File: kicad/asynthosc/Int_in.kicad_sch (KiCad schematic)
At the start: 7 parts, among them J8 AudioJack3, Q1 Q_NPN_BEC, SW10 SW_MEC_5G_LED

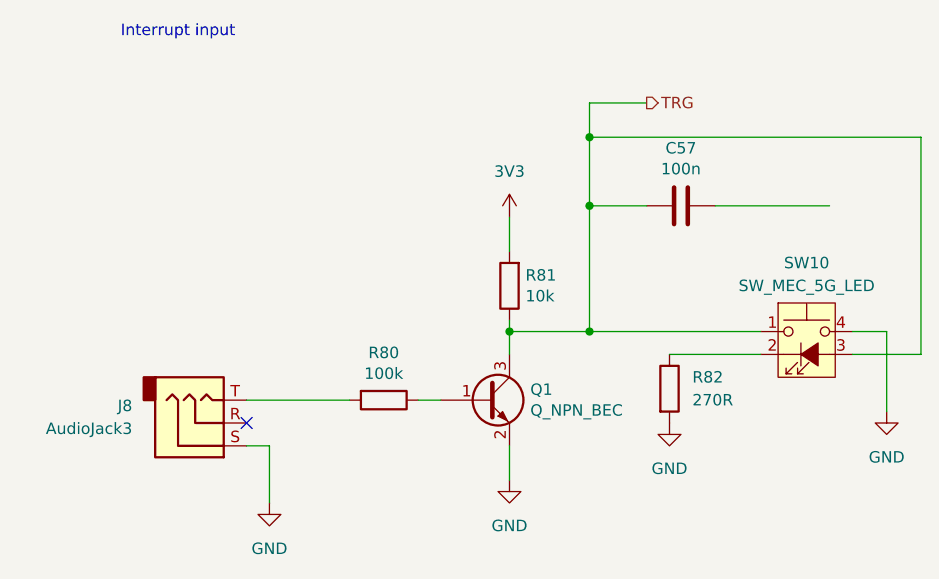
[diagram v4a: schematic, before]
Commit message: bom: update bom for lcsc
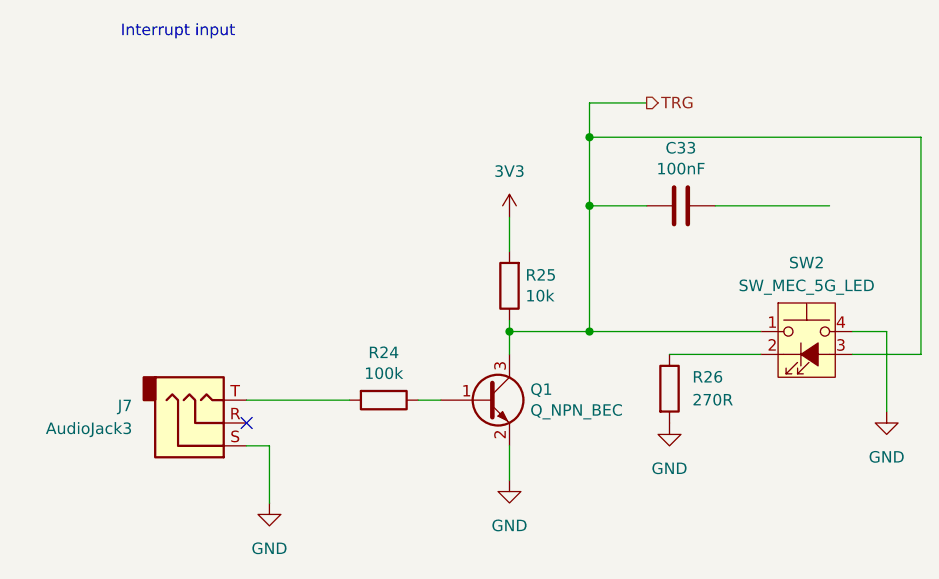
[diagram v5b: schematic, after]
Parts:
- C33: renamed from C57; value 100n -> 100nF
- R24: renamed from R80; RefNum (none) -> _generic_
- R25: renamed from R81; RefNum (none) -> _generic_
- R26: renamed from R82; RefNum (none) -> _generic_
- renumbered J8 to J7, SW10 to SW2
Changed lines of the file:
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@@
 		(dnp no)
 		(fields_autoplaced yes)
-		(property "Reference" "#PWR0137"
+		(property "Reference" "#PWR063"
 			(at 58.42 83.82 0)
 			(effects
@@
 			(project "asynthosc"
 				(path "/d73e377a-a016-415f-8824-91cc6e4907b9/5f8430bb-1923-4d76-b418-f207310879ec/00719137-6b38-42a6-b28f-e4711c0869df"
-					(reference "#PWR0137")
-					(unit 1)
-				)
-				(path "/d73e377a-a016-415f-8824-91cc6e4907b9/5f8430bb-1923-4d76-b418-f207310879ec/1b493739-e50b-4e48-bad0-48b50a96f04e"
-					(reference "#PWR092")
+					(reference "#PWR063")
+					(unit 1)
+				)
+				(path "/d73e377a-a016-415f-8824-91cc6e4907b9/5f8430bb-1923-4d76-b418-f207310879ec/1b493739-e50b-4e48-bad0-48b50a96f04e"
+					(reference "#PWR086")
 					(unit 1)
 				)
@@
 		(dnp no)
 		(fields_autoplaced yes)
-		(property "Reference" "#PWR0140"
+		(property "Reference" "#PWR066"
 			(at 102.87 74.93 0)
 			(effects
@@
 			(project "asynthosc"
 				(path "/d73e377a-a016-415f-8824-91cc6e4907b9/5f8430bb-1923-4d76-b418-f207310879ec/00719137-6b38-42a6-b28f-e4711c0869df"
-					(reference "#PWR0140")
-					(unit 1)
-				)
-				(path "/d73e377a-a016-415f-8824-91cc6e4907b9/5f8430bb-1923-4d76-b418-f207310879ec/1b493739-e50b-4e48-bad0-48b50a96f04e"
-					(reference "#PWR0132")
+					(reference "#PWR066")
+					(unit 1)
+				)
+				(path "/d73e377a-a016-415f-8824-91cc6e4907b9/5f8430bb-1923-4d76-b418-f207310879ec/1b493739-e50b-4e48-bad0-48b50a96f04e"
+					(reference "#PWR089")
 					(unit 1)
 				)
@@
 		(dnp no)
 		(fields_autoplaced yes)
-		(property "Reference" "SW10"
+		(property "Reference" "SW2"
 			(at 118.11 50.8 0)
 			(effects
@@
 			(project "asynthosc"
 				(path "/d73e377a-a016-415f-8824-91cc6e4907b9/5f8430bb-1923-4d76-b418-f207310879ec/00719137-6b38-42a6-b28f-e4711c0869df"
-					(reference "SW10")
-					(unit 1)
-				)
-				(path "/d73e377a-a016-415f-8824-91cc6e4907b9/5f8430bb-1923-4d76-b418-f207310879ec/1b493739-e50b-4e48-bad0-48b50a96f04e"
-					(reference "SW7")
+					(reference "SW2")
+					(unit 1)
+				)
+				(path "/d73e377a-a016-415f-8824-91cc6e4907b9/5f8430bb-1923-4d76-b418-f207310879ec/1b493739-e50b-4e48-bad0-48b50a96f04e"
+					(reference "SW6")
 					(unit 1)
 				)
@@
 		(on_board yes)
 		(dnp no)
-		(property "Reference" "J8"
+		(property "Reference" "J7"
 			(at 43.18 66.6749 0)
 			(effects
@@
 			(project "asynthosc"
 				(path "/d73e377a-a016-415f-8824-91cc6e4907b9/5f8430bb-1923-4d76-b418-f207310879ec/00719137-6b38-42a6-b28f-e4711c0869df"
-					(reference "J8")
-					(unit 1)
-				)
-				(path "/d73e377a-a016-415f-8824-91cc6e4907b9/5f8430bb-1923-4d76-b418-f207310879ec/1b493739-e50b-4e48-bad0-48b50a96f04e"
-					(reference "J5")
+					(reference "J7")
+					(unit 1)
+				)
+				(path "/d73e377a-a016-415f-8824-91cc6e4907b9/5f8430bb-1923-4d76-b418-f207310879ec/1b493739-e50b-4e48-bad0-48b50a96f04e"
+					(reference "J11")
 					(unit 1)
 				)
@@
 		(on_board yes)
 		(dnp no)
-		(property "Reference" "R80"
+		(property "Reference" "R24"
 			(at 71.12 60.7822 90)
 			(effects
@@
 			)
 		)
+		(property "RefNum" "_generic_"
+			(at 71.12 66.04 0)
+			(effects
+				(font
+					(size 1.27 1.27)
+				)
+				(hide yes)
+			)
+		)
 		(pin "2"
 		)
@@
 			(project "asynthosc"
 				(path "/d73e377a-a016-415f-8824-91cc6e4907b9/5f8430bb-1923-4d76-b418-f207310879ec/00719137-6b38-42a6-b28f-e4711c0869df"
-					(reference "R80")
-					(unit 1)
-				)
-				(path "/d73e377a-a016-415f-8824-91cc6e4907b9/5f8430bb-1923-4d76-b418-f207310879ec/1b493739-e50b-4e48-bad0-48b50a96f04e"
-					(reference "R13")
+					(reference "R24")
+					(unit 1)
+				)
+				(path "/d73e377a-a016-415f-8824-91cc6e4907b9/5f8430bb-1923-4d76-b418-f207310879ec/1b493739-e50b-4e48-bad0-48b50a96f04e"
+					(reference "R45")
 					(unit 1)
 				)
@@
 		(dnp no)
 		(fields_autoplaced yes)
-		(property "Reference" "#PWR0139"
+		(property "Reference" "#PWR065"
 			(at 85.09 81.28 0)
 			(effects
@@
 			(project "asynthosc"
 				(path "/d73e377a-a016-415f-8824-91cc6e4907b9/5f8430bb-1923-4d76-b418-f207310879ec/00719137-6b38-42a6-b28f-e4711c0869df"
-					(reference "#PWR0139")
-					(unit 1)
-				)
-				(path "/d73e377a-a016-415f-8824-91cc6e4907b9/5f8430bb-1923-4d76-b418-f207310879ec/1b493739-e50b-4e48-bad0-48b50a96f04e"
-					(reference "#PWR031")
+					(reference "#PWR065")
+					(unit 1)
+				)
+				(path "/d73e377a-a016-415f-8824-91cc6e4907b9/5f8430bb-1923-4d76-b418-f207310879ec/1b493739-e50b-4e48-bad0-48b50a96f04e"
+					(reference "#PWR088")
 					(unit 1)
 				)
@@
 		(dnp no)
 		(fields_autoplaced yes)
-		(property "Reference" "#PWR0138"
+		(property "Reference" "#PWR064"
 			(at 85.09 49.53 0)
 			(effects
@@
 			(project "asynthosc"
 				(path "/d73e377a-a016-415f-8824-91cc6e4907b9/5f8430bb-1923-4d76-b418-f207310879ec/00719137-6b38-42a6-b28f-e4711c0869df"
-					(reference "#PWR0138")
-					(unit 1)
-				)
-				(path "/d73e377a-a016-415f-8824-91cc6e4907b9/5f8430bb-1923-4d76-b418-f207310879ec/1b493739-e50b-4e48-bad0-48b50a96f04e"
-					(reference "#PWR030")
+					(reference "#PWR064")
+					(unit 1)
+				)
+				(path "/d73e377a-a016-415f-8824-91cc6e4907b9/5f8430bb-1923-4d76-b418-f207310879ec/1b493739-e50b-4e48-bad0-48b50a96f04e"
+					(reference "#PWR087")
 					(unit 1)
 				)
@@
 		(dnp no)
 		(fields_autoplaced yes)
-		(property "Reference" "R82"
+		(property "Reference" "R26"
 			(at 105.41 63.4999 0)
 			(effects
@@
 			)
 		)
+		(property "RefNum" "_generic_"
+			(at 102.87 64.77 0)
+			(effects
+				(font
+					(size 1.27 1.27)
+				)
+				(hide yes)
+			)
+		)
 		(pin "1"
 		)
@@
 			(project "asynthosc"
 				(path "/d73e377a-a016-415f-8824-91cc6e4907b9/5f8430bb-1923-4d76-b418-f207310879ec/00719137-6b38-42a6-b28f-e4711c0869df"
-					(reference "R82")
-					(unit 1)
-				)
-				(path "/d73e377a-a016-415f-8824-91cc6e4907b9/5f8430bb-1923-4d76-b418-f207310879ec/1b493739-e50b-4e48-bad0-48b50a96f04e"
-					(reference "R76")
+					(reference "R26")
+					(unit 1)
+				)
+				(path "/d73e377a-a016-415f-8824-91cc6e4907b9/5f8430bb-1923-4d76-b418-f207310879ec/1b493739-e50b-4e48-bad0-48b50a96f04e"
+					(reference "R47")
 					(unit 1)
 				)
@@
 		(dnp no)
 		(fields_autoplaced yes)
-		(property "Reference" "#PWR0141"
+		(property "Reference" "#PWR067"
 			(at 127 73.66 0)
 			(effects
@@
 			(project "asynthosc"
 				(path "/d73e377a-a016-415f-8824-91cc6e4907b9/5f8430bb-1923-4d76-b418-f207310879ec/00719137-6b38-42a6-b28f-e4711c0869df"
-					(reference "#PWR0141")
-					(unit 1)
-				)
-				(path "/d73e377a-a016-415f-8824-91cc6e4907b9/5f8430bb-1923-4d76-b418-f207310879ec/1b493739-e50b-4e48-bad0-48b50a96f04e"
-					(reference "#PWR0130")
+					(reference "#PWR067")
+					(unit 1)
+				)
+				(path "/d73e377a-a016-415f-8824-91cc6e4907b9/5f8430bb-1923-4d76-b418-f207310879ec/1b493739-e50b-4e48-bad0-48b50a96f04e"
+					(reference "#PWR090")
 					(unit 1)
 				)
@@
 		(on_board yes)
 		(dnp no)
-		(property "Reference" "C57"
+		(property "Reference" "C33"
 			(at 104.14 38.0492 90)
 			(effects
@@
 			)
 		)
-		(property "Value" "100n"
+		(property "Value" "100nF"
 			(at 104.14 40.3606 90)
 			(effects
@@
 			(project "asynthosc"
 				(path "/d73e377a-a016-415f-8824-91cc6e4907b9/5f8430bb-1923-4d76-b418-f207310879ec/00719137-6b38-42a6-b28f-e4711c0869df"
-					(reference "C57")
-					(unit 1)
-				)
-				(path "/d73e377a-a016-415f-8824-91cc6e4907b9/5f8430bb-1923-4d76-b418-f207310879ec/1b493739-e50b-4e48-bad0-48b50a96f04e"
-					(reference "C10")
+					(reference "C33")
+					(unit 1)
+				)
+				(path "/d73e377a-a016-415f-8824-91cc6e4907b9/5f8430bb-1923-4d76-b418-f207310879ec/1b493739-e50b-4e48-bad0-48b50a96f04e"
+					(reference "C37")
 					(unit 1)
 				)
@@
 		(on_board yes)
 		(dnp no)
-		(property "Reference" "R81"
+		(property "Reference" "R25"
 			(at 86.868 52.1716 0)
 			(effects
@@
 			)
 		)
+		(property "RefNum" "_generic_"
+			(at 85.09 53.34 0)
+			(effects
+				(font
+					(size 1.27 1.27)
+				)
+				(hide yes)
+			)
+		)
 		(pin "1"
 		)
@@
 			(project "asynthosc"
 				(path "/d73e377a-a016-415f-8824-91cc6e4907b9/5f8430bb-1923-4d76-b418-f207310879ec/00719137-6b38-42a6-b28f-e4711c0869df"
-					(reference "R81")
-					(unit 1)
-				)
-				(path "/d73e377a-a016-415f-8824-91cc6e4907b9/5f8430bb-1923-4d76-b418-f207310879ec/1b493739-e50b-4e48-bad0-48b50a96f04e"
-					(reference "R14")
-					(unit 1)
-				)
+					(reference "R25")
+					(unit 1)
+				)
+				(path "/d73e377a-a016-415f-8824-91cc6e4907b9/5f8430bb-1923-4d76-b418-f207310879ec/1b493739-e50b-4e48-bad0-48b50a96f04e"
+					(reference "R46")
+					(unit 1)
+				)

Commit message: pcb: placing
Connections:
- net GND: now also C33.1
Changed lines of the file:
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@@
+	)
+	(symbol
+		(lib_id "power:GND")
+		(at 120.65 44.45 0)
+		(unit 1)
+		(exclude_from_sim no)
+		(in_bom yes)
+		(on_board yes)
+		(dnp no)
+		(fields_autoplaced yes)
+		(property "Reference" "#PWR028"
+			(at 120.65 50.8 0)
+			(effects
+				(font
+					(size 1.27 1.27)
+				)
+				(hide yes)
+			)
+		)
+		(property "Value" "GND"
+			(at 120.65 49.53 0)
+			(effects
+				(font
+					(size 1.27 1.27)
+				)
+			)
+		)
+		(property "Footprint" ""
+			(at 120.65 44.45 0)
+			(effects
+				(font
+					(size 1.27 1.27)
+				)
+				(hide yes)
+			)
+		)
+		(property "Datasheet" ""
+			(at 120.65 44.45 0)
+			(effects
+				(font
+					(size 1.27 1.27)
+				)
+				(hide yes)
+			)
+		)
+		(property "Description" "Power symbol creates a global label with name \"GND\" , ground"
+			(at 120.65 44.45 0)
+			(effects
+				(font
+					(size 1.27 1.27)
+				)
+				(hide yes)
+			)
+		)
+		(pin "1"
+		)
+		(instances
+			(project "asynthosc"
+				(path "/d73e377a-a016-415f-8824-91cc6e4907b9/5f8430bb-1923-4d76-b418-f207310879ec/00719137-6b38-42a6-b28f-e4711c0869df"
+					(reference "#PWR028")
+					(unit 1)
+				)
+				(path "/d73e377a-a016-415f-8824-91cc6e4907b9/5f8430bb-1923-4d76-b418-f207310879ec/1b493739-e50b-4e48-bad0-48b50a96f04e"
+					(reference "#PWR0147")
+					(unit 1)
+				)
+			)
+		)
 	)
 	(symbol

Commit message: bom: update mfr, serials and lcsc fields
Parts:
- J7: LCSC (none) -> C381132
- Q1: LCSC (none) -> C18221467
- SW2: LCSC (none) -> C2762115
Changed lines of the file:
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@@
 			)
 		)
-		(property "LCSC" ""
+		(property "LCSC" "C2762115"
 			(at 118.11 60.96 0)
 			(effects
@@
 			)
 		)
-		(property "LCSC" ""
+		(property "LCSC" "C381132"
 			(at 50.8 68.58 0)
 			(effects
@@
 			)
 		)
-		(property "LCSC" ""
+		(property "LCSC" "C18221467 "
 			(at 82.55 66.04 0)
 			(effects
